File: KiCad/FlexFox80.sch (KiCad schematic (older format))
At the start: 27 parts, among them J101 DIN-5_180degree, Q101 LMN200B02, Q102 IRF610, U107 LM5134B

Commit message: PCB Updates
PCB is now ready for review. Still needs some silkscreen text added.
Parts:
- added J102: Conn_01x02, Pin_Headers:Pin_Header_Straight_1x02, symbol Connector_Generic:Conn_01x02
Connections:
- net GND: now also J102.1 (Pin_1)
- net at U107.2 (Pilot): now also J102.2 (Pin_2)
- no-connect marks 3 -> 2
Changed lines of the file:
@@
 	1    0    0    -1
 $EndComp
-NoConn ~ 3450 4050
 Wire Wire Line
 	4350 2700 4450 2700
@@
 	1    0    0    -1
 $EndComp
+$Comp
+L Connector_Generic:Conn_01x02 J102
+U 1 1 60A40AAA
+P 3650 4150
+F 0 "J102" H 3650 3950 50  0000 C CNN
+F 1 "Conn_01x02" H 3568 3916 50  0001 C CNN
+F 2 "Pin_Headers:Pin_Header_Straight_1x02" H 3650 4150 50  0001 C CNN
+F 3 "" H 3650 4150 50  0001 C CNN
+F 4 "np" H 3650 4150 50  0001 C CNN "Digi-Key Part No."
+F 5 "np" H 3650 4150 50  0001 C CNN "Link"
+F 6 "np" H 3650 4150 50  0001 C CNN "Manufacturer"
+	1    3650 4150
+	1    0    0    1
+$EndComp
+$Comp
+L FlexFox80-rescue:GND_L8-ARDF-2-Band-MiniTx-rescue #PWR0216
+U 1 1 60A416FC
+P 3450 4150
+F 0 "#PWR0216" H 3450 3900 50  0001 C CNN
+F 1 "GND_L8" H 3450 4000 50  0001 C CNN
+F 2 "" H 3450 4150 50  0000 C CNN
+F 3 "" H 3450 4150 50  0000 C CNN
+	1    3450 4150
+	1    0    0    -1
+$EndComp

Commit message: BOM Updates
Corrections to part information in schematic and BOMs
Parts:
- D101: value Dual Schottky -> MBD54
- D104: value 5V -> ESD; footprint Capacitors_SMD:C_0603 -> Resistors_SMD:R_0603
- U107: Digi-Key Part No. LM5134BMFX/NOPB-ND -> 296-40244-1-ND; Link <a href=\"https://www.digikey.com/products/en?keywords=LM51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 -> <a href=\"https://www.digikey.com/products/en?keywords=296-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
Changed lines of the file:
@@
 F 2 "TO_SOT_Packages_SMD:SOT-23-6-LM5134" H 3300 3100 50  0001 L CNN
 F 3 "" H 3350 3650 50  0001 C CNN
-F 4 "LM5134BMFX/NOPB-ND" H 3150 3950 50  0001 C CNN "Digi-Key Part No."
-F 5 "<a href=\"https://www.digikey.com/products/en?keywords=LM5134BMFX/NOPB-ND\">Link</a>" H 3150 3950 60  0001 C CNN "Link"
+F 4 "296-40244-1-ND" H 3150 3950 50  0001 C CNN "Digi-Key Part No."
+F 5 "<a href=\"https://www.digikey.com/products/en?keywords=296-40244-1-ND\">Link</a>" H 3150 3950 60  0001 C CNN "Link"
 F 6 "Texas Instruments" H 3150 3950 50  0001 C CNN "Manufacturer"
 F 7 "LM5134BMFX/NOPB" H 3150 3950 50  0001 C CNN "Manufacturer PN"
@@
 P 8650 2350
 F 0 "D104" H 8600 2600 50  0000 C CNN
-F 1 "5V" H 8600 2500 50  0000 C CNN
-F 2 "Capacitors_SMD:C_0603" H 8650 2350 50  0001 C CNN
+F 1 "ESD" H 8600 2500 50  0000 C CNN
+F 2 "Resistors_SMD:R_0603" H 8650 2350 50  0001 C CNN
 F 3 "" H 8650 2350 50  0001 C CNN
 F 4 "CG0603MLC-05LECT-ND" H 8650 2350 50  0001 C CNN "Digi-Key Part No."
@@
 P 9150 2100
 F 0 "D101" H 9150 2317 50  0000 C CNN
-F 1 "Dual Schottky" H 9150 2226 50  0001 C CNN
+F 1 "MBD54" H 9150 2226 50  0001 C CNN
 F 2 "TO_SOT_Packages_SMD:SOT-363-0.65" H 9150 2100 50  0001 C CNN
 F 3 "" H 9150 2100 50  0001 C CNN

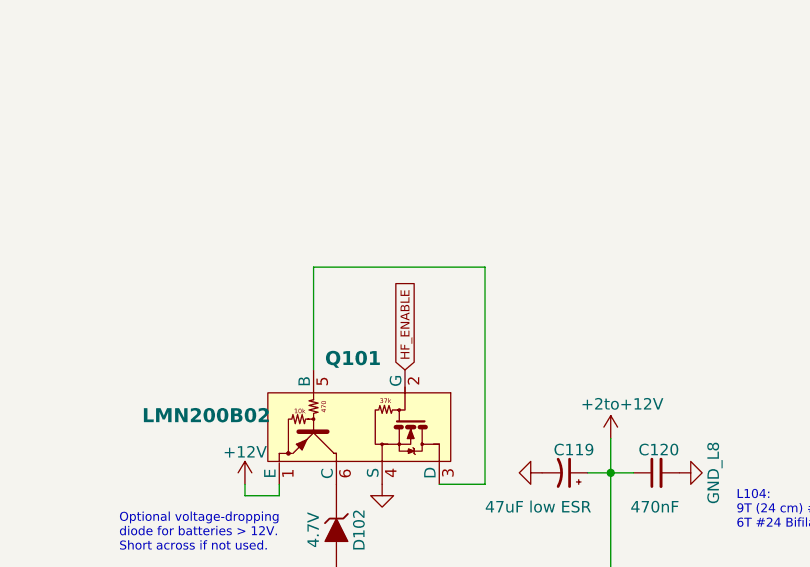
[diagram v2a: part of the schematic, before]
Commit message: AVR128DA48 Redesign
Kicad updates for new FlexFox design
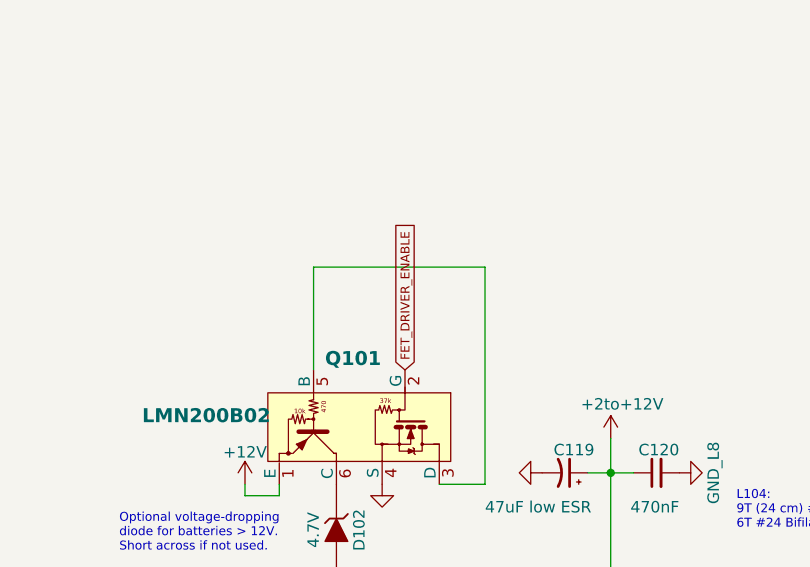
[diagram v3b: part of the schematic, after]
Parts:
- C117: LCSC Part Number (none) -> C337455
- C119: LCSC Part Number (none) -> C122333
- C120, C122: LCSC Part Number (none) -> C342818
- C123, C131: LCSC Part Number (none) -> C2327793
- C126: LCSC Part Number (none) -> C2173329
- C128: LCSC Part Number (none) -> C2439516
- D101: LCSC Part Number (none) -> C152486
- D102: LCSC Part Number (none) -> C151054
- D104: LCSC Part Number (none) -> C2655331
- Q101: LCSC Part Number (none) -> C150757
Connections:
- net HF_ENABLE renamed FET_DRIVER_ENABLE
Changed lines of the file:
@@
 F 7 "C0805C112J5GAC7800" H 5800 3600 50  0001 C CNN "Manufacturer PN"
 F 8 "CAP CER 1100PF 50V NP0 0805" H 5800 3600 50  0001 C CNN "Description"
+F 9 "C2327793" H 5800 3600 50  0001 C CNN "LCSC Part Number"
 	1    5800 3600
 	1    0    0    -1
@@
 CLK1
 Text GLabel 3450 2250 1    39   Input ~ 0
-HF_ENABLE
+FET_DRIVER_ENABLE
 $Comp
 L Device:C_Small C120
@@
 F 7 "08051C474K4Z2A" V 4550 2700 50  0001 C CNN "Manufacturer PN"
 F 8 "CAP CER 0.47UF 100V X7R 0805" V 4550 2700 50  0001 C CNN "Description"
+F 9 "C342818" H 4550 2700 50  0001 C CNN "LCSC Part Number"
 	1    4550 2700
 	0    -1   -1   0
@@
 F 7 "CGA4F2C0G2A182J085AA" H 6500 3600 50  0001 C CNN "Manufacturer PN"
 F 8 "CAP CER 1800PF 100V C0G 0805" H 6500 3600 50  0001 C CNN "Description"
+F 9 "C2173329" H 6500 3600 50  0001 C CNN "LCSC Part Number"
 	1    6500 3600
 	-1   0    0    1
@@
 F 7 "C0805C910J1GAC7800" V 7100 3100 50  0001 C CNN "Manufacturer PN"
 F 8 "CAP CER 91PF 100V NP0 0805" V 7100 3100 50  0001 C CNN "Description"
+F 9 "C2439516" H 7100 3100 50  0001 C CNN "LCSC Part Number"
 	1    7100 3100
 	0    1    1    0
@@
 F 7 "T495X476K020ATE150" V 4150 2700 50  0001 C CNN "Manufacturer PN"
 F 8 "CAP TANT 47UF 10% 20V 2917" V 4150 2700 50  0001 C CNN "Description"
+F 9 "C122333" H 4150 2700 50  0001 C CNN "LCSC Part Number"
 	1    4150 2700
 	0    1    -1   0
@@
 F 7 "CL32A226MAJNNNE" V 3350 3250 50  0001 C CNN "Manufacturer PN"
 F 8 "CAP CER 22UF 25V X5R 1210" V 3350 3250 50  0001 C CNN "Description"
+F 9 "C337455" H 3350 3250 50  0001 C CNN "LCSC Part Number"
 	1    3350 3250
 	0    -1   -1   0
@@
 F 7 "LMN200B02-7" V 3250 2500 50  0001 C CNN "Manufacturer PN"
 F 8 "MCU LOAD SWITCH 200MA SOT-363" V 3250 2500 50  0001 C CNN "Description"
+F 9 "C150757" H 3250 2500 50  0001 C CNN "LCSC Part Number"
 	1    3250 2500
 	0    1    1    0
@@
 F 7 "BZT52C4V7-13-F" H 3150 2950 50  0001 C CNN "Manufacturer PN"
 F 8 "DIODE ZENER 4.7V 500MW SOD123" H 3150 2950 50  0001 C CNN "Description"
+F 9 "C151054" H 3150 2950 50  0001 C CNN "LCSC Part Number"
 	1    3150 2950
 	0    1    1    0
@@
 F 7 "CG0603MLC-05LE" H 8650 2350 50  0001 C CNN "Manufacturer PN"
 F 8 "VARISTOR 0603" H 8650 2350 50  0001 C CNN "Description"
+F 9 "C2655331" H 8650 2350 50  0001 C CNN "LCSC Part Number"
 	1    8650 2350
 	-1   0    0    -1
@@
 F 7 "MBD54DWT1G" H 9150 2100 50  0001 C CNN "Manufacturer PN"
 F 8 "DIODE ARRAY SCHOTTKY 30V SC88" H 9150 2100 50  0001 C CNN "Description"
+F 9 "C152486" H 9150 2100 50  0001 C CNN "LCSC Part Number"
 	1    9150 2100
 	1    0    0    -1
@@
 F 7 "08051C474K4Z2A" V 5550 3400 50  0001 C CNN "Manufacturer PN"
 F 8 "CAP CER 0.47UF 100V X7R 0805" V 5550 3400 50  0001 C CNN "Description"
+F 9 "C342818" H 5550 3400 50  0001 C CNN "LCSC Part Number"
 	1    5550 3400
 	0    -1   -1   0
@@
 F 7 "C0805C112J5GAC7800" H 7500 3600 50  0001 C CNN "Manufacturer PN"
 F 8 "CAP CER 1100PF 50V NP0 0805" H 7500 3600 50  0001 C CNN "Description"
+F 9 "C2327793" H 7500 3600 50  0001 C CNN "LCSC Part Number"
 	1    7500 3600
 	1    0    0    -1

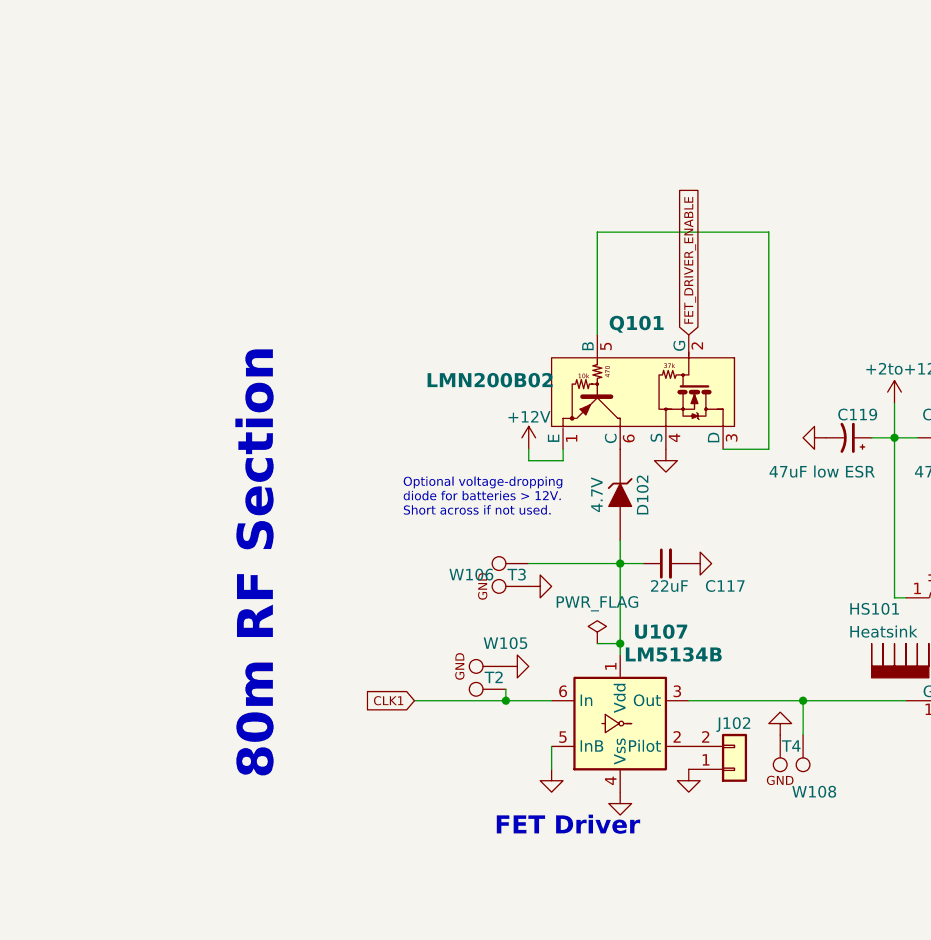
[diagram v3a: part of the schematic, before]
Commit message: Updates for AVR128DA48
o Board changes
o Gerbers updated
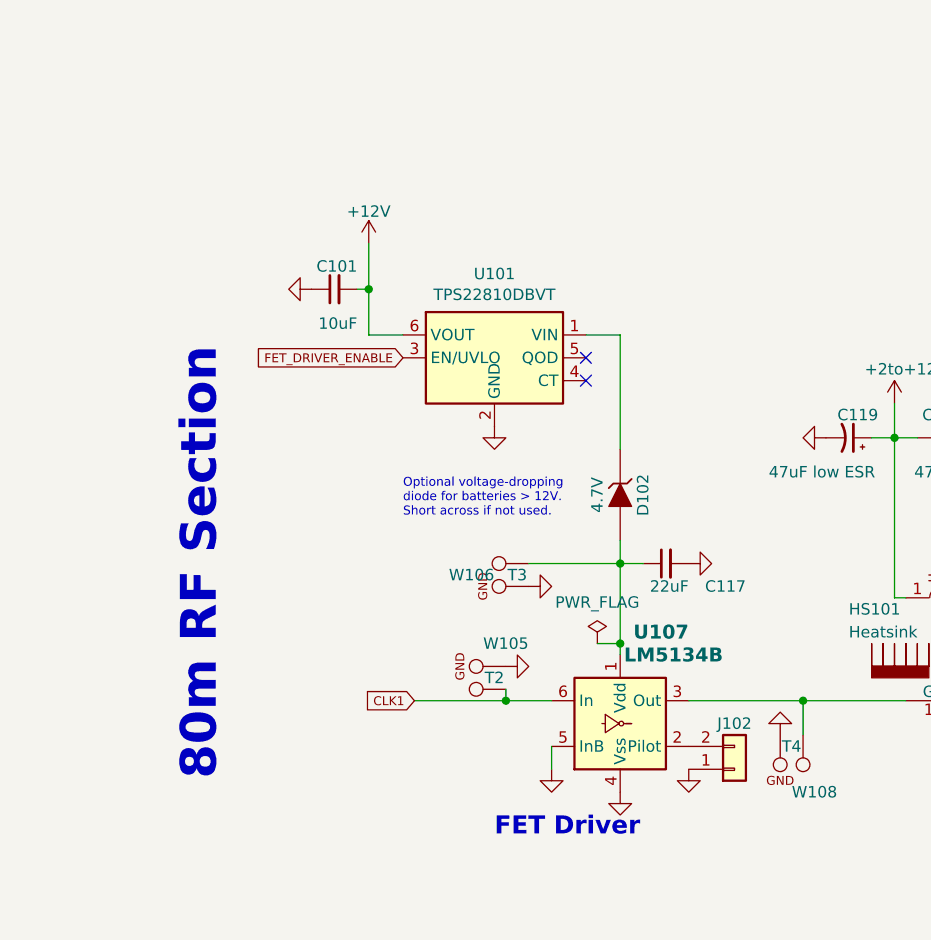
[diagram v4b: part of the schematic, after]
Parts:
- removed Q101: LMN200B02, TO_SOT_Packages_SMD:SOT-363-0.65, symbol Power_Protection:LMN200B01
- added C101: 10uF, Capacitors_SMD:C_0805, symbol Device:C_Small
- added U101: TPS22810DBVT, TO_SOT_Packages_SMD:SOT-23-6, symbol Power_Management:TPS22810DBVT
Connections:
- net +12V: now also C101.2, U101.6 (VOUT)
- net FET_DRIVER_ENABLE: now also U101.3 (EN/UVLO)
- net GND: now also C101.1, U101.2 (GND)
- net at D102.1 (K): now also U101.1 (VIN)
- no-connect marks 2 -> 4
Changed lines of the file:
@@
 L power:+12V #PWR0117
 U 1 1 58BF361E
-P 2750 2750
-F 0 "#PWR0117" H 2750 2600 50  0001 C CNN
-F 1 "+12V" H 2750 2890 50  0000 C CNN
-F 2 "" H 2750 2750 50  0000 C CNN
-F 3 "" H 2750 2750 50  0000 C CNN
-	1    2750 2750
+P 2050 1850
+F 0 "#PWR0117" H 2050 1700 50  0001 C CNN
+F 1 "+12V" H 2050 1990 50  0000 C CNN
+F 2 "" H 2050 1850 50  0000 C CNN
+F 3 "" H 2050 1850 50  0000 C CNN
+	1    2050 1850
 	1    0    0    -1
 $EndComp
@@
 F1 "file591BC95F.sch" 60
 $EndSheet
-Text Notes 1650 4200 1    157  ~ 31
+Text Notes 1400 4200 1    157  ~ 31
 80m RF Section
 Wire Wire Line
@@
 $EndComp
 Connection ~ 850  7350
-Wire Wire Line
-	3600 2750 3800 2750
-Wire Wire Line
-	3800 2750 3800 1800
-Wire Wire Line
-	3800 1800 3050 1800
-Wire Wire Line
-	3050 1800 3050 2250
 $Comp
 L FlexFox80-rescue:GND_L8-ARDF-2-Band-MiniTx-rescue #PWR0123
 U 1 1 5A7B67DA
-P 3350 2750
-F 0 "#PWR0123" H 3350 2500 50  0001 C CNN
-F 1 "GND_L8" H 3500 2600 50  0001 C CNN
-F 2 "" H 3350 2750 50  0000 C CNN
-F 3 "" H 3350 2750 50  0000 C CNN
-	1    3350 2750
-	1    0    0    -1
-$EndComp
-Wire Wire Line
-	2750 2750 2750 2800
-Wire Wire Line
-	2750 2800 2900 2800
-Wire Wire Line
-	2900 2800 2900 2750
+P 2600 2650
+F 0 "#PWR0123" H 2600 2400 50  0001 C CNN
+F 1 "GND_L8" H 2750 2500 50  0001 C CNN
+F 2 "" H 2600 2650 50  0000 C CNN
+F 3 "" H 2600 2650 50  0000 C CNN
+	1    2600 2650
+	1    0    0    -1
+$EndComp
 Connection ~ 3150 3250
 $Comp
@@
 Text GLabel 2250 3850 0    39   Input ~ 0
 CLK1
-Text GLabel 3450 2250 1    39   Input ~ 0
+Text GLabel 2200 2350 0    39   Input ~ 0
 FET_DRIVER_ENABLE
 $Comp
@@
 	0    -1   -1   0
 $EndComp
-$Comp
-L Power_Protection:LMN200B01 Q101
-U 1 1 5C64951A
-P 3250 2500
-F 0 "Q101" V 2950 2350 61  0000 L CNB
-F 1 "LMN200B02" V 3200 1550 61  0000 L CNB
-F 2 "TO_SOT_Packages_SMD:SOT-363-0.65" H 3265 2300 50  0001 L CNN
-F 3 "https://www.diodes.com/assets/Datasheets/ds30658.pdf" H 3265 2300 50  0001 L CNN
-F 4 "LMN200B02DICT-ND" H 3250 2500 50  0001 C CNN "Digi-Key Part No."
-F 5 "<a href=\"https://www.digikey.com/products/en?keywords=LMN200B02DICT-ND\">Link</a>" H 3250 2500 60  0001 C CNN "Link"
-F 6 "Diodes Incorporated" V 3250 2500 50  0001 C CNN "Manufacturer"
-F 7 "LMN200B02-7" V 3250 2500 50  0001 C CNN "Manufacturer PN"
-F 8 "MCU LOAD SWITCH 200MA SOT-363" V 3250 2500 50  0001 C CNN "Description"
-F 9 "C150757" H 3250 2500 50  0001 C CNN "LCSC Part Number"
-	1    3250 2500
-	0    1    1    0
-$EndComp
 Text Notes 2200 3050 0    39   ~ 0
 Optional voltage-dropping\ndiode for batteries > 12V.\nShort across if not used.
@@
 	1    0    0    -1
 $EndComp
+NoConn ~ 3000 2450
+NoConn ~ 3000 2350
+Wire Wire Line
+	3000 2250 3150 2250
+Wire Wire Line
+	3150 2250 3150 2750
+Wire Wire Line
+	2050 1850 2050 2050
+Wire Wire Line
+	2050 2250 2200 2250
+$Comp
+L Device:C_Small C101
+U 1 1 62881448
+P 1900 2050
+F 0 "C101" V 2000 1950 50  0000 L CNN
+F 1 "10uF" V 1750 1950 50  0000 L CNN
+F 2 "Capacitors_SMD:C_0805" H 1900 2050 50  0001 C CNN
+F 3 "" H 1900 2050 50  0001 C CNN
+F 4 "490-5523-1-ND" H 1900 2050 50  0001 C CNN "Digi-Key Part No."
+F 5 "<a href=\"https://www.digikey.com/products/en?keywords=490-5523-1-ND\">Link</a>" H 1900 2050 60  0001 C CNN "Link"
+F 6 "Murata" V 1900 2050 50  0001 C CNN "Manufacturer"
+F 7 "GRM21BR61E106KA73L" V 1900 2050 50  0001 C CNN "Manufacturer PN"
+F 8 "CAP CER 10UF 25V X5R 0805" V 1900 2050 50  0001 C CNN "Description"
+F 9 "C84416" H 1900 2050 50  0001 C CNN "LCSC Part Number"
+	1    1900 2050
+	0    -1   -1   0
+$EndComp
+Wire Wire Line
+	2000 2050 2050 2050
+Connection ~ 2050 2050
+Wire Wire Line
+	2050 2050 2050 2250
+$Comp
+L FlexFox80-rescue:GND_L8-ARDF-2-Band-MiniTx-rescue #PWR0127
+U 1 1 628838B3
+P 1800 2050
+F 0 "#PWR0127" H 1800 1800 50  0001 C CNN
+F 1 "GND_L8" H 1800 1900 50  0001 C CNN
+F 2 "" H 1800 2050 50  0000 C CNN
+F 3 "" H 1800 2050 50  0000 C CNN
+	1    1800 2050
+	0    1    1    0
+$EndComp
+$Comp
+L Power_Management:TPS22810DBVT U101
+U 1 1 628D7F12
+P 2600 2350
+F 0 "U101" H 2600 2717 50  0000 C CNN
+F 1 "TPS22810DBVT" H 2600 2626 50  0000 C CNN
+F 2 "TO_SOT_Packages_SMD:SOT-23-6" H 2600 1650 50  0001 C CNN
+F 3 "http://www.ti.com/lit/ds/symlink/tps22810.pdf" H 2600 2350 50  0001 C CNN
+F 4 "296-45304-1-ND" H 2600 2350 50  0001 C CNN "Digi-Key Part No."
+F 5 "<a href=\"https://www.digikey.com/products/en?keywords=296-45304-1-ND\">Link</a>" H 2600 2350 50  0001 C CNN "Link"
+F 6 "Texas Instruments" H 2600 2350 50  0001 C CNN "Manufacturer"
+F 7 "TPS22810DBVT" H 2600 2350 50  0001 C CNN "Manufacturer PN"
+F 8 "Power Switch/Driver 1:1 N-Channel 2A SOT-23-6" H 2600 2350 50  0001 C CNN "Description"
+F 9 "C2680364" H 2600 2350 50  0001 C CNN "LCSC Part Number"
+	1    2600 2350
+	1    0    0    -1
+$EndComp

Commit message: Updates
o Added fan control
o Fixed pinout for load switch device
o Updated gerbers
o Updated BOM
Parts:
- C101: Manufacturer Murata -> Murata Electronics
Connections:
- net +12V: now also U101.1 (VIN); no longer U101.6 (VOUT)
- net at D102.1 (K): now also U101.6 (VOUT); no longer U101.1 (VIN)

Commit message: Updates
o BOM updates
o Gerber updates
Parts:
- U107: LCSC Part Number (none) -> C2677086
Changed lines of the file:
@@
 F 7 "LM5134BMFX/NOPB" H 3150 3950 50  0001 C CNN "Manufacturer PN"
 F 8 "IC GATE DRVR LOW-SIDE SOT23-6" H 3150 3950 50  0001 C CNN "Description"
+F 9 "C2677086" H 3150 3950 50  0001 C CNN "LCSC Part Number"
 	1    3150 3950
 	1    0    0    -1

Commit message: Gerber Updates
o Changed parts for C128, L203 and L204 to help with parts shortages
o Updated footprints
o Updated schematic
o Updated BOM
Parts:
- C128: footprint Capacitors_SMD:C_0805 -> Capacitors_SMD:C_0603; Description CAP CER 91PF 100V NP0 0805 -> CAP CER 91PF 100V NP0 0603; Digi-Key Part No. 399-17459-1-ND -> 478-10247-1-ND; LCSC Part Number C2439516 -> (none); Link <a href=\"https://www.digikey.com/products/en?keywords=399-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 -> <a href=\"https://www.digikey.com/products/en?keywords=478-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; Manufacturer KEMET -> KYOCERA AVX; Manufacturer PN C0805C910J1GAC7800 -> 06031U910FAT2A
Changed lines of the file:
@@
 F 0 "C128" V 7000 3000 50  0000 L CNN
 F 1 "91pF" V 7200 3000 50  0000 L CNN
-F 2 "Capacitors_SMD:C_0805" H 7100 3100 50  0001 C CNN
+F 2 "Capacitors_SMD:C_0603" H 7100 3100 50  0001 C CNN
 F 3 "" H 7100 3100 50  0000 C CNN
-F 4 "399-17459-1-ND" H 7100 3100 50  0001 C CNN "Digi-Key Part No."
-F 5 "<a href=\"https://www.digikey.com/products/en?keywords=399-17459-1-ND\">Link</a>" H 7100 3100 60  0001 C CNN "Link"
-F 6 "KEMET" V 7100 3100 50  0001 C CNN "Manufacturer"
-F 7 "C0805C910J1GAC7800" V 7100 3100 50  0001 C CNN "Manufacturer PN"
-F 8 "CAP CER 91PF 100V NP0 0805" V 7100 3100 50  0001 C CNN "Description"
-F 9 "C2439516" H 7100 3100 50  0001 C CNN "LCSC Part Number"
+F 4 "478-10247-1-ND" H 7100 3100 50  0001 C CNN "Digi-Key Part No."
+F 5 "<a href=\"https://www.digikey.com/products/en?keywords=478-10247-1-ND\">Link</a>" H 7100 3100 60  0001 C CNN "Link"
+F 6 "KYOCERA AVX" V 7100 3100 50  0001 C CNN "Manufacturer"
+F 7 "06031U910FAT2A" V 7100 3100 50  0001 C CNN "Manufacturer PN"
+F 8 "CAP CER 91PF 100V NP0 0603" V 7100 3100 50  0001 C CNN "Description"
 	1    7100 3100
 	0    1    1    0

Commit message: Gerber Update
o Corrected dimensions of U203
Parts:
- C128: LCSC Part Number (none) -> C2170042
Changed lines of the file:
@@
 F 7 "06031U910FAT2A" V 7100 3100 50  0001 C CNN "Manufacturer PN"
 F 8 "CAP CER 91PF 100V NP0 0603" V 7100 3100 50  0001 C CNN "Description"
+F 9 "C2170042" H 7100 3100 50  0001 C CNN "LCSC Part Number"
 	1    7100 3100
 	0    1    1    0
